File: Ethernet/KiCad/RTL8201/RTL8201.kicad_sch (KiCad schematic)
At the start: 23 parts, among them J1 Conn_01x02_Male, U1 RTL8201F, Y1 25MHz

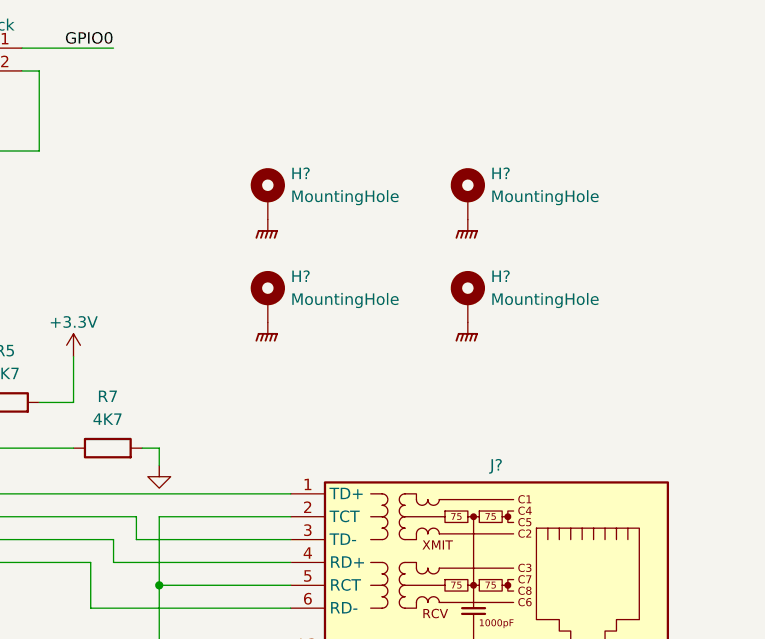
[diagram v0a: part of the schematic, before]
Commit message: CH340G
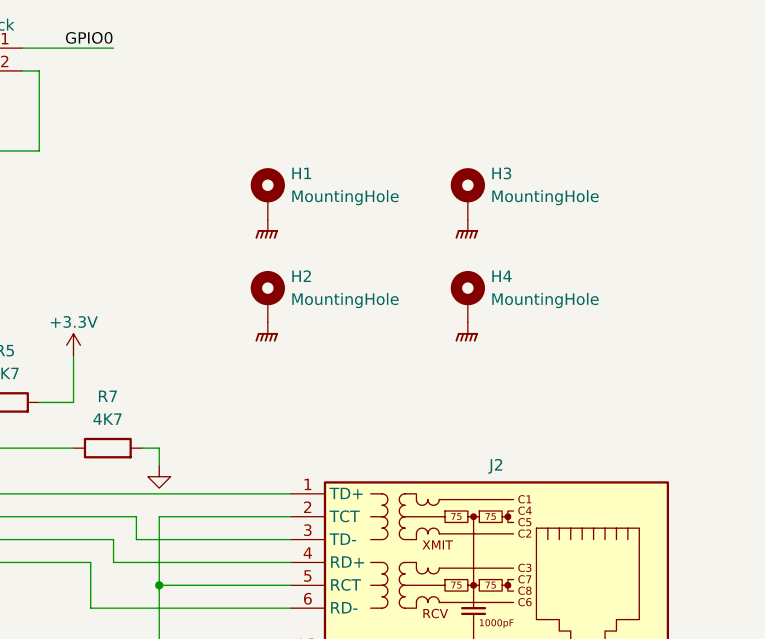
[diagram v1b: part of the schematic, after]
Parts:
- gave numbers to parts that had none: 5
